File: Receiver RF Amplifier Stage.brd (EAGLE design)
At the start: 115.5 x 84.8 mm, 16 parts, among them T1 2N2222

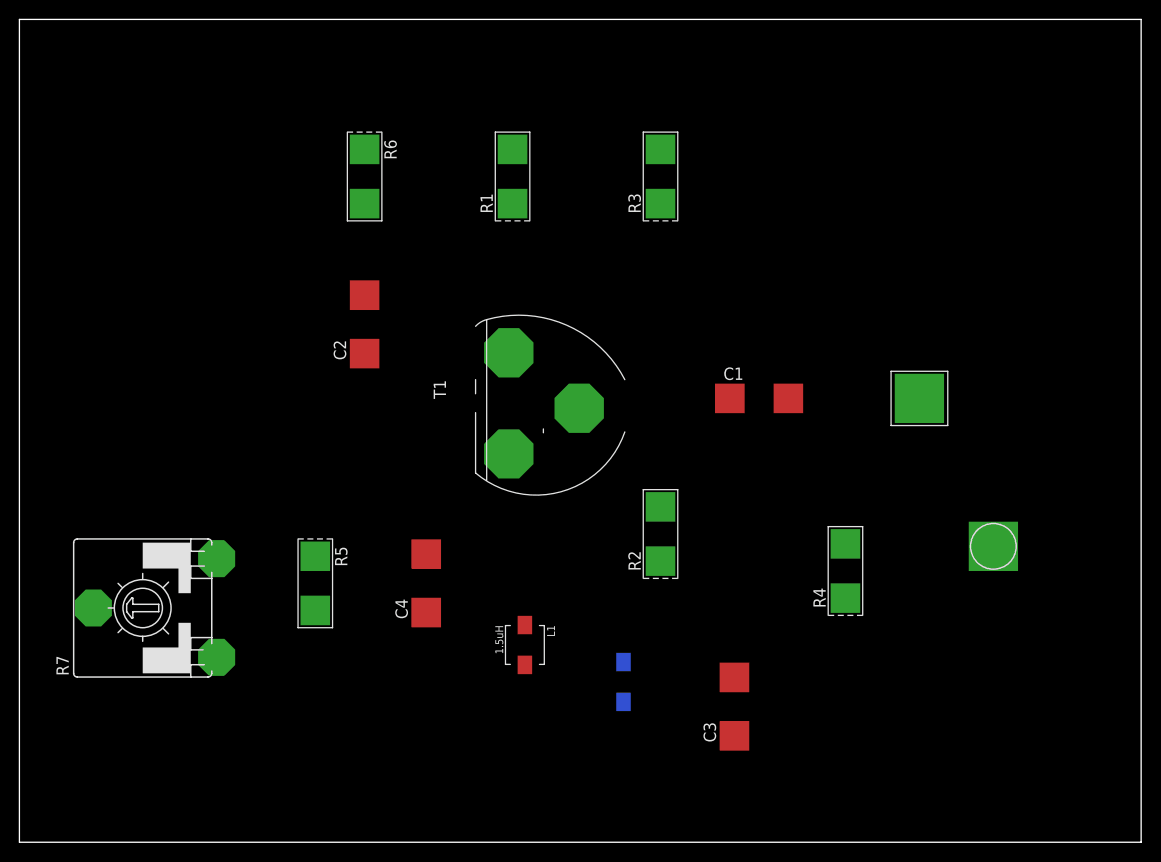
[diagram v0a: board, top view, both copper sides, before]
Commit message: Updated schematic to have a bifilar winding
Updated schematic to have a bifilar winding or center tapped
transformer.

Also starting to work on the board.

On branch master
Your branch is up-to-date with 'origin/master'.

Changes to be committed:
       modified:   Receiver RF Amplifier Stage.b#1
       modified:   Receiver RF Amplifier Stage.b#2
       modified:   Receiver RF Amplifier Stage.b#3
       modified:   Receiver RF Amplifier Stage.b#4
       modified:   Receiver RF Amplifier Stage.b#5
       new file:   Receiver RF Amplifier Stage.b#6
       new file:   Receiver RF Amplifier Stage.b#7
       new file:   Receiver RF Amplifier Stage.b#8
       new file:   Receiver RF Amplifier Stage.b#9
       modified:   Receiver RF Amplifier Stage.brd
       modified:   Receiver RF Amplifier Stage.s#1
       modified:   Receiver RF Amplifier Stage.s#2
       modified:   Receiver RF Amplifier Stage.s#3
       modified:   Receiver RF Amplifier Stage.s#4
       modified:   Receiver RF Amplifier Stage.s#5
       modified:   Receiver RF Amplifier Stage.s#6
       modified:   Receiver RF Amplifier Stage.s#7
       modified:   Receiver RF Amplifier Stage.s#8
       new file:   Receiver RF Amplifier Stage.s#9
       modified:   Receiver RF Amplifier Stage.sch
       modified:   broadband_receiver_rf_amp.png
       modified:   eagle.epf
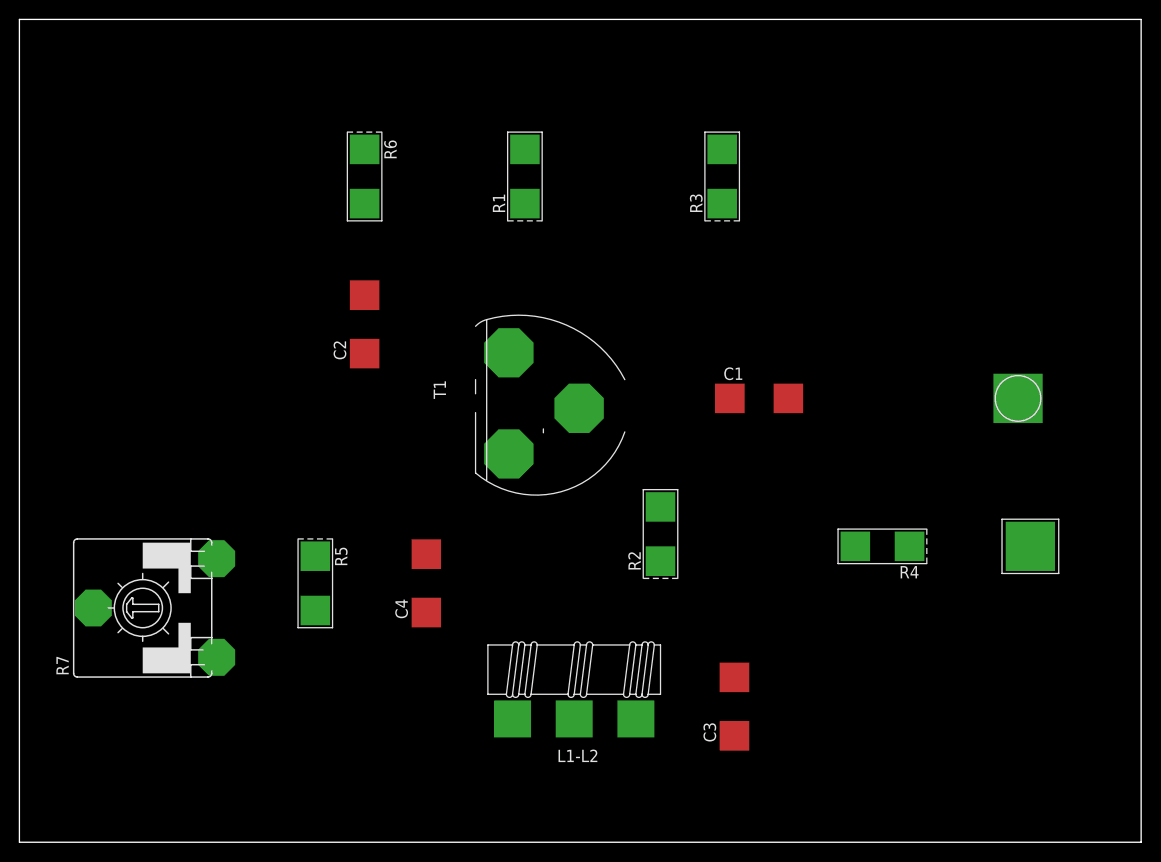
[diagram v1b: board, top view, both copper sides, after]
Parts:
- removed H1: RF Signal In, jim_muppet_parts:PAD-SQUARE
- removed L1, L2: 1.5uH, SparkFun-Passives:INDUCTOR-SRP4020
- added AC-SIGNAL: IN FROM ?, jim_muppet_parts:PAD-SQUARE
- added L1-L2: T37-43_BIFILAR_TORIODBIFILAR-COIL/TRANSFORMER, jim_muppet_parts:T37-43_BIFILAR_TOROID
- moved P+1 19.1 mm to (104.1, 30.5)
- moved R3 6.35 mm to (72.4, 68.6)
- moved R4 4.58 mm to (88.9, 30.5), turned to 180 degrees
- moved R1 1.27 mm to (52.1, 68.6)
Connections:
- net +12V: now also R4.P$2; no longer C1.2
- net N$3: now also T1.1; no longer T1.3
- net N$5: now also L1-L2.C2A, T1.3; no longer L1.P$1, T1.1
- net N$6: now also L1-L2.C3A; no longer L1.P$2, L2.P$1
- net N$7: now also L1-L2.C1A; no longer L2.P$2
- net N$9: now also AC-SIGNAL.PAD, C1.2; no longer H1.PAD, R4.P$2
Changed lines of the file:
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@@
 <attribute name="VALUE" x="45.085" y="22.733" size="1.27" layer="27" font="vector" rot="R90"/>
 </element>
-<element name="L1" library="SparkFun-Passives" package="INDUCTOR-SRP4020" value="1.5uH" x="52.07" y="20.32" smashed="yes" rot="R270">
-<attribute name="NAME" x="54.356" y="22.352" size="0.8128" layer="25" font="vector" ratio="15" rot="R270"/>
-<attribute name="VALUE" x="49.022" y="22.352" size="0.8128" layer="25" font="vector" ratio="15" rot="R270"/>
-</element>
-<element name="L2" library="SparkFun-Passives" package="INDUCTOR-SRP4020" value="1.5uH" x="62.23" y="16.51" smashed="yes" rot="MR270">
-<attribute name="NAME" x="59.944" y="18.542" size="0.8128" layer="26" font="vector" ratio="15" rot="MR270"/>
-<attribute name="VALUE" x="65.278" y="18.542" size="0.8128" layer="26" font="vector" ratio="15" rot="MR270"/>
-</element>
-<element name="R1" library="jim_muppet_parts" package="RESITOR-MUPPET" value="100R" x="50.8" y="68.58" smashed="yes" rot="R90">
-<attribute name="NAME" x="48.768" y="64.77" size="1.27" layer="25" rot="R90"/>
-<attribute name="PROD_ID" value="MUP-RES" x="81.28" y="106.68" size="1.778" layer="27" rot="R90" display="off"/>
-<attribute name="VALUE" x="54.102" y="64.643" size="1.27" layer="27" rot="R90"/>
+<element name="R1" library="jim_muppet_parts" package="RESITOR-MUPPET" value="100R" x="52.07" y="68.58" smashed="yes" rot="R90">
+<attribute name="NAME" x="50.038" y="64.77" size="1.27" layer="25" rot="R90"/>
+<attribute name="PROD_ID" value="MUP-RES" x="82.55" y="106.68" size="1.778" layer="27" rot="R90" display="off"/>
+<attribute name="VALUE" x="55.372" y="64.643" size="1.27" layer="27" rot="R90"/>
 </element>
 <element name="R2" library="jim_muppet_parts" package="RESITOR-MUPPET" value="2.2K" x="66.04" y="31.75" smashed="yes" rot="R90">
@@
 <attribute name="VALUE" x="69.342" y="27.813" size="1.27" layer="27" rot="R90"/>
 </element>
-<element name="R3" library="jim_muppet_parts" package="RESITOR-MUPPET" value="1K" x="66.04" y="68.58" smashed="yes" rot="R90">
-<attribute name="NAME" x="64.008" y="64.77" size="1.27" layer="25" rot="R90"/>
-<attribute name="PROD_ID" value="MUP-RES" x="106.68" y="86.36" size="1.778" layer="27" rot="R90" display="off"/>
-<attribute name="VALUE" x="69.342" y="64.643" size="1.27" layer="27" rot="R90"/>
+<element name="R3" library="jim_muppet_parts" package="RESITOR-MUPPET" value="1K" x="72.39" y="68.58" smashed="yes" rot="R90">
+<attribute name="NAME" x="70.358" y="64.77" size="1.27" layer="25" rot="R90"/>
+<attribute name="PROD_ID" value="MUP-RES" x="113.03" y="86.36" size="1.778" layer="27" rot="R90" display="off"/>
+<attribute name="VALUE" x="75.692" y="64.643" size="1.27" layer="27" rot="R90"/>
 </element>
-<element name="R4" library="jim_muppet_parts" package="RESITOR-MUPPET" value="10R" x="85.09" y="27.94" smashed="yes" rot="R90">
-<attribute name="NAME" x="83.058" y="24.13" size="1.27" layer="25" rot="R90"/>
-<attribute name="PROD_ID" value="MUP-RES" x="125.73" y="55.88" size="1.778" layer="27" rot="R90" display="off"/>
-<attribute name="VALUE" x="88.392" y="24.003" size="1.27" layer="27" rot="R90"/>
+<element name="R4" library="jim_muppet_parts" package="RESITOR-MUPPET" value="10R" x="88.9" y="30.48" smashed="yes" rot="R180">
+<attribute name="NAME" x="92.71" y="28.448" size="1.27" layer="25" rot="R180"/>
+<attribute name="PROD_ID" value="MUP-RES" x="60.96" y="71.12" size="1.778" layer="27" rot="R180" display="off"/>
+<attribute name="VALUE" x="92.837" y="33.782" size="1.27" layer="27" rot="R180"/>
 </element>
 <element name="R5" library="jim_muppet_parts" package="RESITOR-MUPPET" value="100R" x="30.48" y="26.67" smashed="yes" rot="R270">
@@
 <attribute name="VALUE" x="44.577" y="49.149" size="1.27" layer="27" ratio="10" rot="R270"/>
 </element>
-<element name="P+1" library="jim_muppet_parts" package="POWER-IN-PAD" value="+12V" x="92.71" y="45.72" smashed="yes"/>
-<element name="H1" library="jim_muppet_parts" package="PAD-SQUARE" package3d_urn="urn:adsk.eagle:package:14295/1" value="RF Signal In" x="100.33" y="30.48" smashed="yes"/>
+<element name="L1-L2" library="jim_muppet_parts" package="T37-43_BIFILAR_TOROID" value="T37-43_BIFILAR_TORIODBIFILAR-COIL/TRANSFORMER" x="57.15" y="17.78" smashed="yes" rot="R90">
+<attribute name="NAME" x="59.69" y="9.525" size="1.27" layer="25" rot="R180"/>
+<attribute name="VALUE" x="59.69" y="22.86" size="1.27" layer="27" rot="R180"/>
+</element>
+<element name="P+1" library="jim_muppet_parts" package="POWER-IN-PAD" value="+12V" x="104.14" y="30.48" smashed="yes"/>
+<element name="AC-SIGNAL" library="jim_muppet_parts" package="PAD-SQUARE" package3d_urn="urn:adsk.eagle:package:14295/1" value="IN FROM ?" x="102.87" y="45.72" smashed="yes">
+<attribute name="SPICEPREFIX" value="A" x="102.87" y="45.72" size="1.778" layer="27" display="off"/>
+</element>
 </elements>
 <signals>
 <signal name="N$1">
-<contactref element="T1" pad="2"/>
 <contactref element="C1" pad="1"/>
 <contactref element="R2" pad="P$2"/>
 <contactref element="R3" pad="P$1"/>
-<wire x1="57.658" y1="44.704" x2="66.04" y2="65.786" width="0" layer="19" extent="1-1"/>
-<wire x1="73.191" y1="45.72" x2="66.04" y2="65.786" width="0" layer="19" extent="1-1"/>
+<contactref element="T1" pad="2"/>
+<wire x1="73.191" y1="45.72" x2="72.39" y2="65.786" width="0" layer="19" extent="1-1"/>
 <wire x1="66.04" y1="34.544" x2="73.191" y2="45.72" width="0" layer="19" extent="1-1"/>
+<wire x1="57.658" y1="44.704" x2="66.04" y2="34.544" width="0" layer="19" extent="1-1"/>
 </signal>
 <signal name="GND">
@@
 <contactref element="R3" pad="P$2"/>
 <contactref element="R1" pad="P$2"/>
-<wire x1="50.8" y1="71.374" x2="66.04" y2="71.374" width="0" layer="19" extent="1-1"/>
-<wire x1="35.56" y1="71.374" x2="50.8" y2="71.374" width="0" layer="19" extent="1-1"/>
+<wire x1="52.07" y1="71.374" x2="72.39" y2="71.374" width="0" layer="19" extent="1-1"/>
+<wire x1="35.56" y1="71.374" x2="52.07" y2="71.374" width="0" layer="19" extent="1-1"/>
 <wire x1="30.48" y1="23.876" x2="35.56" y2="71.374" width="0" layer="19" extent="1-1"/>
 <wire x1="20.32" y1="19.05" x2="30.48" y2="23.876" width="0" layer="19" extent="1-1"/>
@@
 </signal>
 <signal name="N$3">
-<contactref element="T1" pad="3"/>
+<contactref element="C2" pad="1"/>
+<contactref element="T1" pad="1"/>
 <contactref element="R1" pad="P$1"/>
-<contactref element="C2" pad="1"/>
-<wire x1="50.419" y1="50.419" x2="50.8" y2="65.786" width="0" layer="19" extent="1-1"/>
-<wire x1="35.56" y1="50.331" x2="50.419" y2="50.419" width="0" layer="19" extent="1-1"/>
+<wire x1="35.56" y1="50.331" x2="52.07" y2="65.786" width="0" layer="19" extent="1-1"/>
+<wire x1="50.419" y1="40.005" x2="35.56" y2="50.331" width="0" layer="19" extent="1-1"/>
 </signal>
 <signal name="N$4">
@@
 </signal>
 <signal name="N$5">
-<contactref element="T1" pad="1"/>
-<contactref element="L1" pad="P$1"/>
-<wire x1="52.07" y1="22.37" x2="50.419" y2="40.005" width="0" layer="19" extent="1-1"/>
+<contactref element="T1" pad="3"/>
+<contactref element="L1-L2" pad="C2A"/>
+<wire x1="57.15" y1="12.7" x2="50.419" y2="50.419" width="0" layer="19" extent="1-1"/>
 </signal>
 <signal name="N$6">
-<contactref element="L1" pad="P$2"/>
-<contactref element="L2" pad="P$1"/>
 <contactref element="C4" pad="1"/>
-<wire x1="52.07" y1="18.27" x2="41.91" y2="23.661" width="0" layer="19" extent="1-1"/>
-<wire x1="62.23" y1="18.56" x2="52.07" y2="18.27" width="0" layer="19" extent="1-16"/>
+<contactref element="L1-L2" pad="C3A"/>
+<wire x1="50.8" y1="12.7" x2="41.91" y2="23.661" width="0" layer="19" extent="1-1"/>
 </signal>
 <signal name="N$7">
 <contactref element="R2" pad="P$1"/>
 <contactref element="C3" pad="2"/>
-<contactref element="L2" pad="P$2"/>
 <contactref element="R4" pad="P$1"/>
-<wire x1="73.66" y1="16.979" x2="85.09" y2="25.146" width="0" layer="19" extent="1-1"/>
+<contactref element="L1-L2" pad="C1A"/>
+<wire x1="73.66" y1="16.979" x2="91.694" y2="30.48" width="0" layer="19" extent="1-1"/>
 <wire x1="66.04" y1="28.956" x2="73.66" y2="16.979" width="0" layer="19" extent="1-1"/>
-<wire x1="62.23" y1="14.46" x2="73.66" y2="16.979" width="0" layer="19" extent="1-16"/>
+<wire x1="63.5" y1="12.7" x2="66.04" y2="28.956" width="0" layer="19" extent="1-1"/>
 </signal>
 <signal name="N$8">
@@
 <wire x1="20.32" y1="29.21" x2="30.48" y2="29.464" width="0" layer="19" extent="1-1"/>
 </signal>
+<signal name="+12V">
+<contactref element="R4" pad="P$2"/>
+<contactref element="P+1" pad="VCC"/>
+<wire x1="104.14" y1="30.48" x2="86.106" y2="30.48" width="0" layer="19" extent="1-1"/>
+</signal>
 <signal name="N$9">
-<contactref element="R4" pad="P$2"/>
-<contactref element="H1" pad="PAD"/>
-<wire x1="100.33" y1="30.48" x2="85.09" y2="30.734" width="0" layer="19" extent="1-1"/>
-</signal>
-<signal name="+12V">
+<contactref element="AC-SIGNAL" pad="PAD"/>
 <contactref element="C1" pad="2"/>
-<contactref element="P+1" pad="VCC"/>
-<wire x1="92.71" y1="45.72" x2="79.209" y2="45.72" width="0" layer="19" extent="1-1"/>
+<wire x1="102.87" y1="45.72" x2="79.209" y2="45.72" width="0" layer="19" extent="1-1"/>
 </signal>
 </signals>

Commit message: Lots of changes.
Recreated the IF Schema and a new board to look like the photo

On branch master
Changes to be committed:
       modified:   Receiver RF Amplifier Stage.b#1
       modified:   Receiver RF Amplifier Stage.b#2
       modified:   Receiver RF Amplifier Stage.b#3
       modified:   Receiver RF Amplifier Stage.b#4
       modified:   Receiver RF Amplifier Stage.b#5
       modified:   Receiver RF Amplifier Stage.b#6
       modified:   Receiver RF Amplifier Stage.b#7
       modified:   Receiver RF Amplifier Stage.b#8
       modified:   Receiver RF Amplifier Stage.b#9
       modified:   Receiver RF Amplifier Stage.brd
       modified:   Receiver RF Amplifier Stage.s#1
       modified:   Receiver RF Amplifier Stage.s#2
       modified:   Receiver RF Amplifier Stage.s#3
       modified:   Receiver RF Amplifier Stage.s#4
       modified:   Receiver RF Amplifier Stage.s#5
       modified:   Receiver RF Amplifier Stage.s#6
       modified:   Receiver RF Amplifier Stage.s#7
       modified:   Receiver RF Amplifier Stage.s#8
       modified:   Receiver RF Amplifier Stage.s#9
       modified:   Receiver RF Amplifier Stage.sch
       modified:   Sudden_XCVR_IF_Module.b#1
       modified:   Sudden_XCVR_IF_Module.b#2
       modified:   Sudden_XCVR_IF_Module.b#3
       modified:   Sudden_XCVR_IF_Module.b#4
       modified:   Sudden_XCVR_IF_Module.b#5
       modified:   Sudden_XCVR_IF_Module.b#6
       modified:   Sudden_XCVR_IF_Module.b#7
       modified:   Sudden_XCVR_IF_Module.brd
       new file:   Sudden_XCVR_IF_Module_Schematic_like_board_layout.b#1
       new file:   Sudden_XCVR_IF_Module_Schematic_like_board_layout.b#2
       new file:   Sudden_XCVR_IF_Module_Schematic_like_board_layout.b#3
       new file:   Sudden_XCVR_IF_Module_Schematic_like_board_layout.brd
       new file:   Sudden_XCVR_IF_Module_Schematic_like_board_layout.s#1
       new file:   Sudden_XCVR_IF_Module_Schematic_like_board_layout.s#2
       new file:   Sudden_XCVR_IF_Module_Schematic_like_boa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
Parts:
- removed R7: 100R, jim_muppet_parts:CA14V
- added AC-SIGNAL-OUT: Output from Center Wiper, jim_muppet_parts:PAD-SQUARE
- added R11: (no value), jim_muppet_parts:POT-TRIMM-4
- T1: device jim_muppet_parts:TO92 -> jim_muppet_parts:2N2222-TO18
- moved P+1 51.3 mm to (59.2, 5.84)
- moved AC-SIGNAL 44.0 mm to (59.2, 40.6)
- moved R3 39.9 mm to (45.0, 39.6)
- moved R6 36.7 mm to (10.9, 41.4), turned to 0 degrees
- moved R4 36.3 mm to (56.4, 14.2), turned to 0 degrees
- moved R1 31.9 mm to (32.8, 43.2), turned to 180 degrees
- moved C3 29.6 mm to (45.0, 6.86)
- moved C1 25.0 mm to (56.1, 30.7)
- moved L1-L2 23.6 mm to (33.5, 17.3), flipped to the bottom, turned to 270 degrees
- moved R2 23.3 mm to (45.0, 21.8)
- moved T1 22.1 mm to (35.6, 34.5), flipped to the bottom
- moved C2 20.1 mm to (22.1, 38.4)
- moved C4 20.1 mm to (21.8, 25.7)
- moved R5 16.8 mm to (13.7, 26.2)
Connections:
- new net N$3: AC-SIGNAL-OUT.PAD, R11.S
- net GND: now also R11.E; no longer R7.A
- net N$8: now also R11.A; no longer R7.E
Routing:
- net N$7: track 0.00 -> 33.0 mm
- net N$1: track 0.00 -> 28.8 mm
- net N$12: track 0.00 -> 23.1 mm
- net N$8: track 0.00 -> 15.1 mm
- net N$9: track 0.00 -> 9.92 mm
- net N$3: track 0.00 -> 9.14 mm
- net N$5: track 0.00 -> 8.89 mm
- net N$4: track 0.00 -> 8.67 mm
- net +12V: track 0.00 -> 8.38 mm
- net N$6: track 0.00 -> 6.73 mm
- added copper zone on layer 1, net GND
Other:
- board size 115.5 x 84.8 mm -> 69.6 x 47.9 mm
- board text added: "Broadband RF Amplifier - N6QW"
- board text added: "EagleCAD Jim - AE0BZ 12/23/18"
